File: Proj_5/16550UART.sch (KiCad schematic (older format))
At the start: 1 part

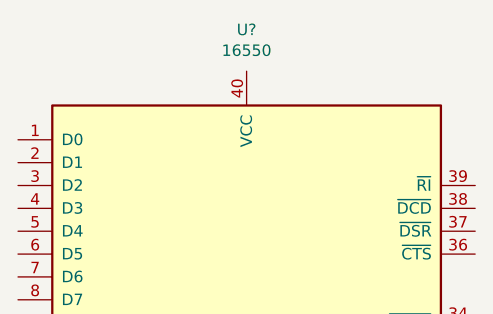
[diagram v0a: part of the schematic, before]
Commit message: Added address decoding
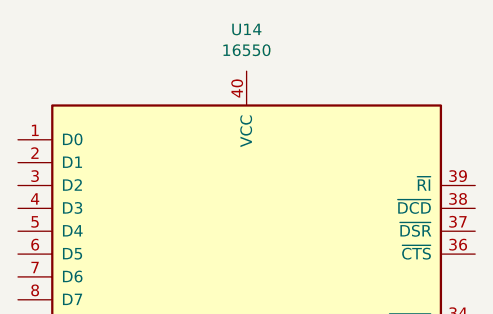
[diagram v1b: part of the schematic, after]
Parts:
- gave numbers to parts that had none: 1
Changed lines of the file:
@@
 $EndDescr
 $Comp
-L Interface_UART:16550 U?
+L Interface_UART:16550 U14
 U 1 1 5EA9C406
 P 4300 3300
-F 0 "U?" H 4300 5181 50  0000 C CNN
+F 0 "U14" H 4300 5181 50  0000 C CNN
 F 1 "16550" H 4300 5090 50  0000 C CNN
 F 2 "Package_DIP:DIP-40_W15.24mm" H 4300 3300 50  0001 C CIN

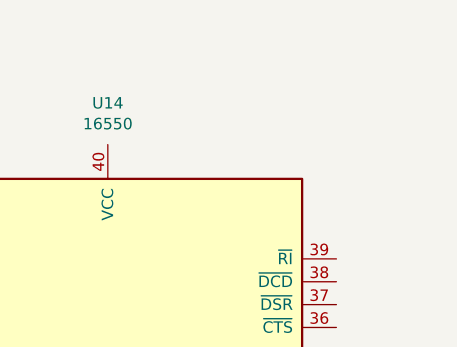
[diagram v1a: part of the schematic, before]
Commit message: Added Caps to Each Vcc per desc.
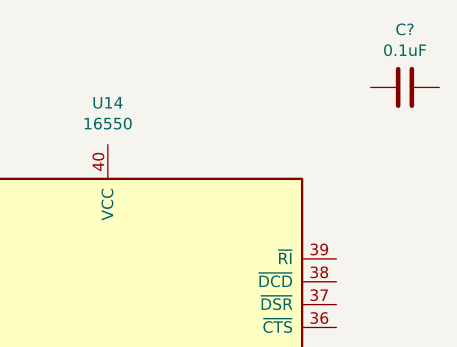
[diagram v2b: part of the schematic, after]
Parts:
- added C?: 0.1uF, symbol Device:C
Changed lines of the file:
@@
 $Descr A2 23386 16535
 encoding utf-8
-Sheet 6 11
+Sheet 5 11
 Title ""
 Date ""
@@
 	1    0    0    -1
 $EndComp
+$Comp
+L Device:C C?
+U 1 1 5EA6B70D
+P 5600 1350
+AR Path="/5EA98353/5EA6B70D" Ref="C?"  Part="1"
+AR Path="/5EA98A67/5EA6B70D" Ref="C?"  Part="1"
+F 0 "C?" V 5348 1350 50  0000 C CNN
+F 1 "0.1uF" V 5439 1350 50  0000 C CNN
+F 2 "" H 5638 1200 50  0001 C CNN
+F 3 "~" H 5600 1350 50  0001 C CNN
+	1    5600 1350
+	0    1    1    0
+$EndComp
 $EndSCHEMATC
